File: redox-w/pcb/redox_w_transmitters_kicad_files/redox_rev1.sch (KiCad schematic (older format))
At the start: 85 parts, among them K0 KEYSW, K1 KEYSW, K10 KEYSW, K11 KEYSW, K12 KEYSW, K13 KEYSW, K14 KEYSW, K15 KEYSW, K16 KEYSW, K2 KEYSW, K20 KEYSW, K21 KEYSW, K22 KEYSW, K23 KEYSW, K24 KEYSW, K25 KEYSW, K26 KEYSW, K3 KEYSW, K30 KEYSW, K31 KEYSW, K32 KEYSW, K33 KEYSW, K34 KEYSW, K35 KEYSW, K36 KEYSW, K4 KEYSW, K40 KEYSW, K41 KEYSW, K42 KEYSW, K43 KEYSW, K44 KEYSW, K45 KEYSW, K46 KEYSW, K5 KEYSW, K6 KEYSW

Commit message: PCB Roughly Finished - All Labels In Place
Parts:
- added R4, R5: 4.7k, Resistor_SMD:R_0805_2012Metric_Pad1.15x1.40mm_HandSolder, symbol Device:R
- renumbered C_1 to C2, Q_LEFT1 to Q1, U_LEFT2 to U1
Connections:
- net SCL2: now also R5.1
- net SDA2: now also R4.2
- net VCC: now also R4.1, R5.2
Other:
- moved on the sheet: C2
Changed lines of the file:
@@
 	6800 5750 6500 5750
 $Comp
-L Power_Management:LTC4412xS6 U_LEFT2
+L Power_Management:LTC4412xS6 U1
 U 1 1 5E8D8C59
 P 7200 5850
-F 0 "U_LEFT2" H 7200 6431 50  0000 C CNN
+F 0 "U1" H 7200 6431 50  0000 C CNN
 F 1 "LTC4412xS6" H 7200 6340 50  0000 C CNN
 F 2 "Package_TO_SOT_SMD:TSOT-23-6" H 7850 5500 50  0001 C CNN
@@
 Connection ~ 8200 5750
 $Comp
-L Transistor_FET:DMG2301L Q_LEFT1
+L Transistor_FET:DMG2301L Q1
 U 1 1 5EAB6B43
 P 6800 5250
-F 0 "Q_LEFT1" V 7142 5250 50  0000 C CNN
+F 0 "Q1" V 7142 5250 50  0000 C CNN
 F 1 "DMG2301L" V 7051 5250 50  0000 C CNN
 F 2 "Package_TO_SOT_SMD:SOT-23" H 7000 5175 50  0001 L CIN
@@
 	0    1    -1   0
 $EndComp
-Wire Wire Line
-	6050 5000 6050 4850
-Connection ~ 6050 5000
-Wire Wire Line
-	6050 5150 6050 5000
 $Comp
 L power:GND #PWR0110
 U 1 1 5EA69E1C
-P 5750 5000
-F 0 "#PWR0110" H 5750 4750 50  0001 C CNN
-F 1 "GND" V 5755 4872 50  0000 R CNN
-F 2 "" H 5750 5000 50  0001 C CNN
-F 3 "" H 5750 5000 50  0001 C CNN
-	1    5750 5000
-	0    1    -1   0
-$EndComp
-$Comp
-L Device:C C_1
+P 5750 4850
+F 0 "#PWR0110" H 5750 4600 50  0001 C CNN
+F 1 "GND" V 5755 4722 50  0000 R CNN
+F 2 "" H 5750 4850 50  0001 C CNN
+F 3 "" H 5750 4850 50  0001 C CNN
+	1    5750 4850
+	0    1    -1   0
+$EndComp
+$Comp
+L Device:C C2
 U 1 1 5EA69E16
-P 5900 5000
-F 0 "C_1" V 5750 5000 50  0000 C CNN
-F 1 "1 μF" V 5650 5000 50  0000 C CNN
-F 2 "Capacitor_SMD:C_0805_2012Metric_Pad1.15x1.40mm_HandSolder" H 5938 4850 50  0001 C CNN
-F 3 "~" H 5900 5000 50  0001 C CNN
-	1    5900 5000
+P 5900 4850
+F 0 "C2" V 5750 4850 50  0000 C CNN
+F 1 "1 μF" V 5650 4850 50  0000 C CNN
+F 2 "Capacitor_SMD:C_0805_2012Metric_Pad1.15x1.40mm_HandSolder" H 5938 4700 50  0001 C CNN
+F 3 "~" H 5900 4850 50  0001 C CNN
+	1    5900 4850
 	0    1    -1   0
 $EndComp
@@
 NoConn ~ 3650 4950
 NoConn ~ 3650 4850
-Text GLabel 3650 5350 0    60   Input ~ 0
+Text GLabel 3100 5350 0    60   Input ~ 0
 SCL2
-Text GLabel 3650 5250 0    60   Input ~ 0
+Text GLabel 3100 5250 0    60   Input ~ 0
 SDA2
 $Comp
@@
 $EndComp
 $Comp
-L power:VCC #PWR?
+L power:VCC #PWR0112
 U 1 1 5E8D360D
 P 6100 6250
-F 0 "#PWR?" H 6100 6100 50  0001 C CNN
+F 0 "#PWR0112" H 6100 6100 50  0001 C CNN
 F 1 "VCC" H 6118 6423 50  0000 C CNN
 F 2 "" H 6100 6250 50  0001 C CNN
@@
 	8900 5150 8900 5350
 Connection ~ 8300 5150
+Connection ~ 6050 4850
+Wire Wire Line
+	6050 4850 6050 5150
+$Comp
+L power:VCC #PWR0114
+U 1 1 5E88315B
+P 3350 5650
+F 0 "#PWR0114" H 3350 5500 50  0001 C CNN
+F 1 "VCC" H 3367 5823 50  0000 C CNN
+F 2 "" H 3350 5650 50  0001 C CNN
+F 3 "" H 3350 5650 50  0001 C CNN
+	1    3350 5650
+	1    0    0    1
+$EndComp
+$Comp
+L power:VCC #PWR0121
+U 1 1 5E883161
+P 3200 5650
+F 0 "#PWR0121" H 3200 5500 50  0001 C CNN
+F 1 "VCC" H 3217 5823 50  0000 C CNN
+F 2 "" H 3200 5650 50  0001 C CNN
+F 3 "" H 3200 5650 50  0001 C CNN
+	1    3200 5650
+	1    0    0    1
+$EndComp
+Wire Wire Line
+	3350 5300 3350 5250
+Wire Wire Line
+	3350 5250 3650 5250
+Wire Wire Line
+	3350 5650 3350 5600
+$Comp
+L Device:R R4
+U 1 1 5E883170
+P 3350 5450
+F 0 "R4" H 3420 5496 50  0000 L CNN
+F 1 "4.7k" H 3420 5405 50  0000 L CNN
+F 2 "Resistor_SMD:R_0805_2012Metric_Pad1.15x1.40mm_HandSolder" V 3280 5450 50  0001 C CNN
+F 3 "~" H 3350 5450 50  0001 C CNN
+	1    3350 5450
+	1    0    0    1
+$EndComp
+$Comp
+L Device:R R5
+U 1 1 5E883176
+P 3200 5500
+F 0 "R5" H 3270 5454 50  0000 L CNN
+F 1 "4.7k" H 3270 5545 50  0000 L CNN
+F 2 "Resistor_SMD:R_0805_2012Metric_Pad1.15x1.40mm_HandSolder" V 3130 5500 50  0001 C CNN
+F 3 "~" H 3200 5500 50  0001 C CNN
+	1    3200 5500
+	-1   0    0    -1
+$EndComp
+Wire Wire Line
+	3200 5350 3650 5350
+Wire Wire Line
+	3350 5250 3100 5250
+Connection ~ 3350 5250
+Wire Wire Line
+	3100 5350 3200 5350
+Connection ~ 3200 5350
 $EndSCHEMATC

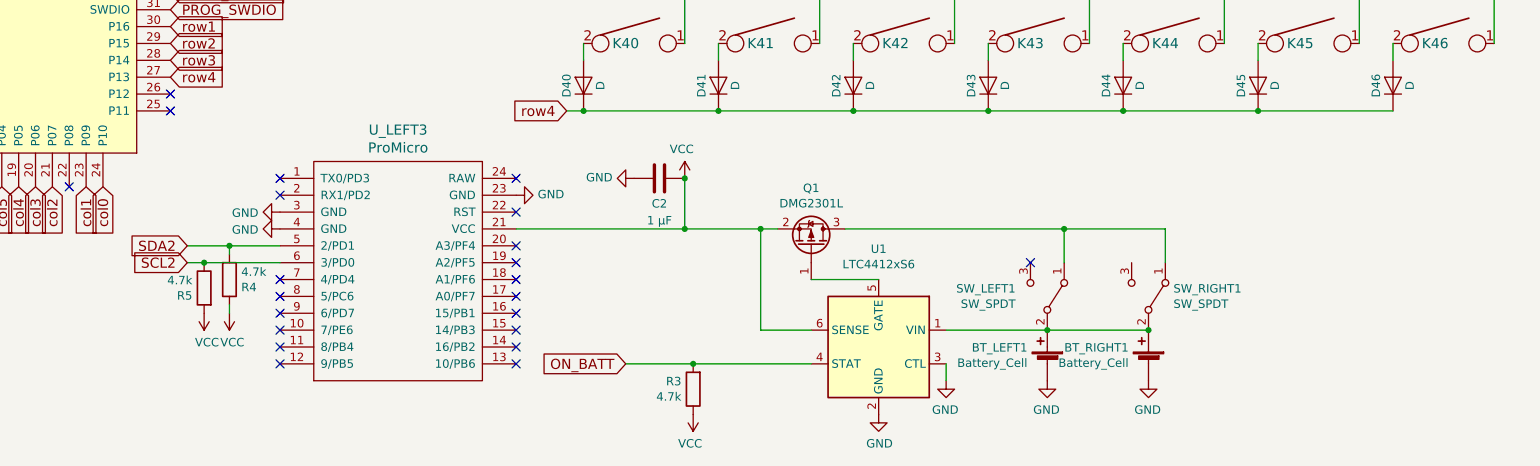
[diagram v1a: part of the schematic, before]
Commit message: Tweaking After Checking JLcPCB Submission
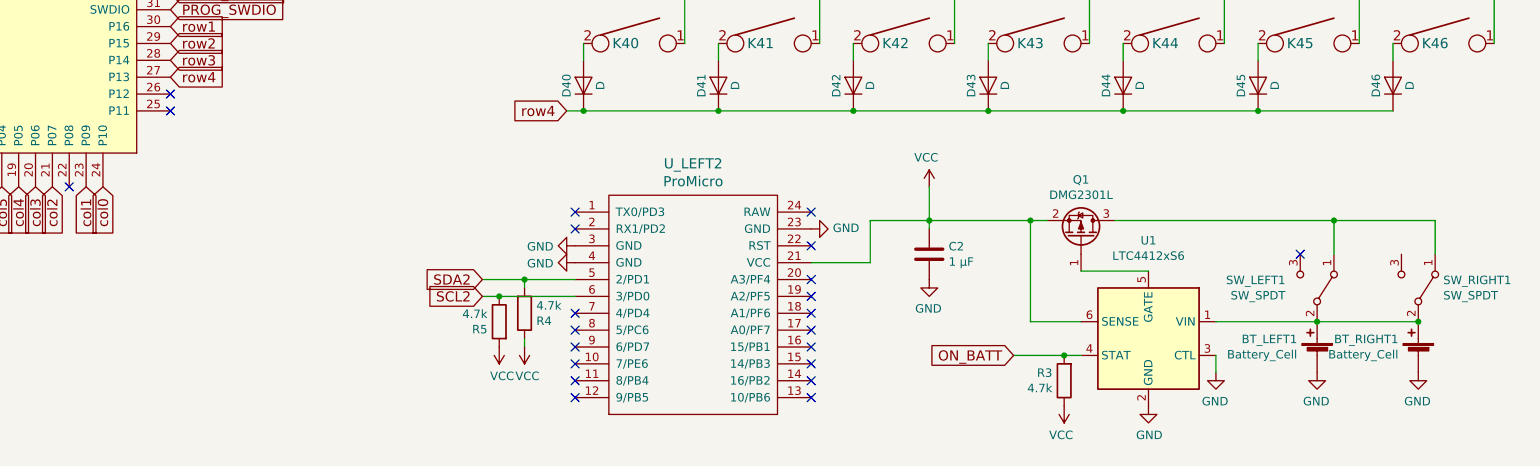
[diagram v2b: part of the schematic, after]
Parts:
- renumbered U_LEFT3 to U_LEFT2
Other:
- moved on the sheet: BT_LEFT1, BT_RIGHT1, C2, Q1, R3, R4, R5, SW_LEFT1, SW_RIGHT1, U1, U_LEFT2

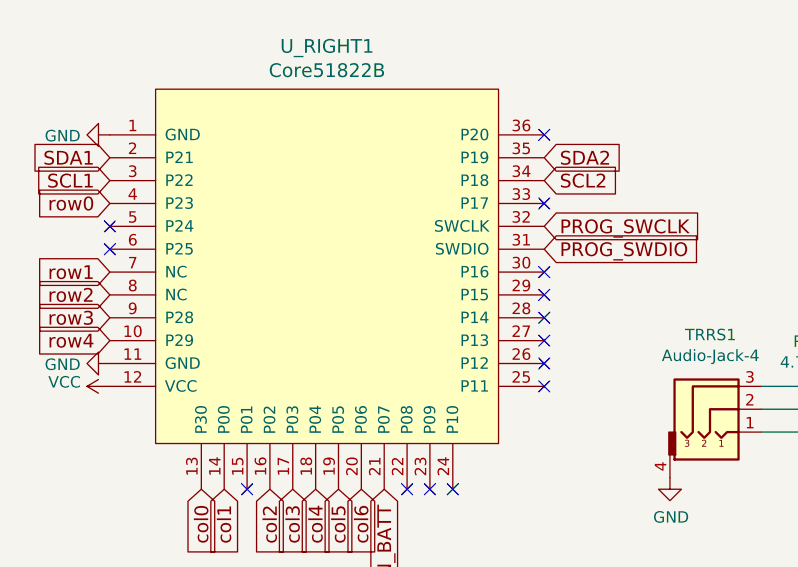
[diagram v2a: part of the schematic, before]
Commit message: Fixed Bug Where row1 and row2 Were on NC's
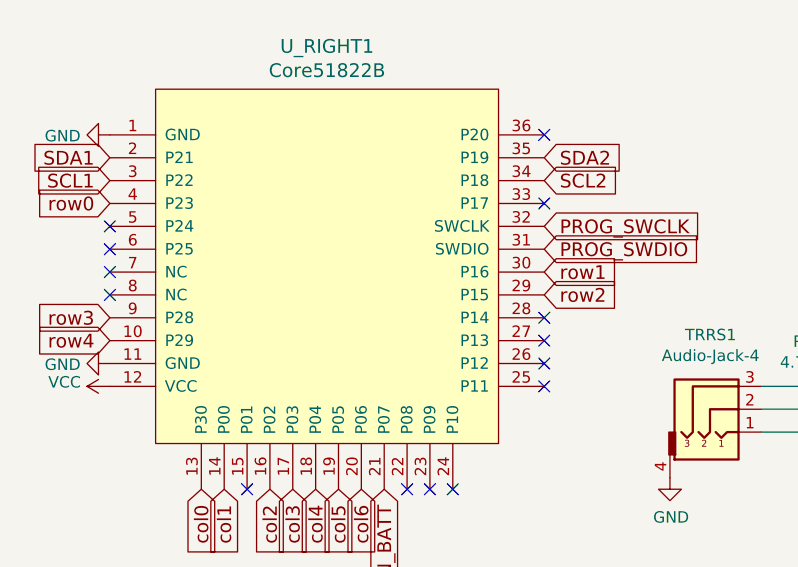
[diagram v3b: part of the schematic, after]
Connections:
- net row1: now also U_RIGHT1.30 (P16); no longer U_RIGHT1.7 (NC)
- net row2: now also U_RIGHT1.29 (P15); no longer U_RIGHT1.8 (NC)
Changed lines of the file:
@@
 NoConn ~ 1100 1400
 NoConn ~ 1100 1500
-Text GLabel 1100 1700 0    60   Input ~ 0
+Text GLabel 3000 1700 2    60   Input ~ 0
 row2
-Text GLabel 1100 1600 0    60   Input ~ 0
+Text GLabel 3000 1600 2    60   Input ~ 0
 row1
 Text GLabel 1100 1300 0    60   Input ~ 0
@@
 col0
 NoConn ~ 3000 1800
-NoConn ~ 3000 1700
-NoConn ~ 3000 1600
 NoConn ~ 3000 1000
 Text GLabel 3000 1500 2    60   Input ~ 0
@@
 SCL2
 NoConn ~ 1100 3650
-$Comp
-L redox_rev1-rescue:Core51822B-core51822b U_RIGHT1
-U 1 1 5B82A47C
-P 2050 1500
-F 0 "U_RIGHT1" H 2050 2387 60  0000 C CNN
-F 1 "Core51822B" H 2050 2281 60  0000 C CNN
-F 2 "redox_w_footprints:MY-YJ-14015-Module" H 2050 1600 60  0001 C CNN
-F 3 "" H 2050 1600 60  0001 C CNN
-	1    2050 1500
-	1    0    0    -1
-$EndComp
 Wire Wire Line
 	4450 1800 4450 1850
@@
 F 3 "" H 2050 3950 60  0001 C CNN
 	1    2050 3850
-	1    0    0    -1
-$EndComp
-$Comp
-L redox_wired:ProMicro U_LEFT2
-U 1 1 5E7DC5DE
-P 6100 5600
-F 0 "U_LEFT2" H 6100 6437 60  0000 C CNN
-F 1 "ProMicro" H 6100 6331 60  0000 C CNN
-F 2 "redox_w_footprints:ArduinoProMicro" V 7150 3100 60  0001 C CNN
-F 3 "" V 7150 3100 60  0001 C CNN
-	1    6100 5600
 	1    0    0    -1
 $EndComp
@@
 NoConn ~ 5400 6150
 NoConn ~ 6800 5050
-NoConn ~ 6800 5250
 NoConn ~ 6800 5450
 NoConn ~ 6800 5550
@@
 Text GLabel 5350 4450 0    60   Input ~ 0
 row4
+$Comp
+L redox_wired:ProMicro U_LEFT2
+U 1 1 5E7DC5DE
+P 6100 5600
+F 0 "U_LEFT2" H 6100 6437 60  0000 C CNN
+F 1 "ProMicro" H 6100 6331 60  0000 C CNN
+F 2 "redox_w_footprints:ArduinoProMicro" V 7150 3100 60  0001 C CNN
+F 3 "" V 7150 3100 60  0001 C CNN
+	1    6100 5600
+	1    0    0    -1
+$EndComp
+NoConn ~ 6800 5250
+$Comp
+L redox_rev1-rescue:Core51822B-core51822b U_RIGHT1
+U 1 1 5B82A47C
+P 2050 1500
+F 0 "U_RIGHT1" H 2050 2387 60  0000 C CNN
+F 1 "Core51822B" H 2050 2281 60  0000 C CNN
+F 2 "redox_w_footprints:MY-YJ-14015-Module" H 2050 1600 60  0001 C CNN
+F 3 "" H 2050 1600 60  0001 C CNN
+	1    2050 1500
+	1    0    0    -1
+$EndComp
+NoConn ~ 1100 1600
+NoConn ~ 1100 1700
 $EndSCHEMATC
